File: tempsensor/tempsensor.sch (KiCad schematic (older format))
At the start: 64 parts

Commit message: Added testpads to tempsensor, added missing TWI lines to EEPROM.
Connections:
- wire segments 228 -> 241
- no-connect marks 13 -> 17
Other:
- moved on the sheet: TP?
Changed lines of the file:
@@
 L Connector:TestPoint TP?
 U 1 1 5EB7CF1E
-P 4900 5400
-F 0 "TP?" V 4854 5588 50  0000 L CNN
-F 1 "SCL" V 4945 5588 50  0000 L CNN
-F 2 "" H 5100 5400 50  0001 C CNN
-F 3 "~" H 5100 5400 50  0001 C CNN
-	1    4900 5400
+P 5450 5550
+F 0 "TP?" V 5404 5738 50  0000 L CNN
+F 1 "SCL" V 5495 5738 50  0000 L CNN
+F 2 "" H 5650 5550 50  0001 C CNN
+F 3 "~" H 5650 5550 50  0001 C CNN
+	1    5450 5550
 	0    1    1    0
 $EndComp
@@
 L Connector:TestPoint TP?
 U 1 1 5EB7D977
-P 4900 5600
-F 0 "TP?" V 4854 5788 50  0000 L CNN
-F 1 "SDA" V 4945 5788 50  0000 L CNN
-F 2 "" H 5100 5600 50  0001 C CNN
-F 3 "~" H 5100 5600 50  0001 C CNN
-	1    4900 5600
+P 5450 5750
+F 0 "TP?" V 5404 5938 50  0000 L CNN
+F 1 "SDA" V 5495 5938 50  0000 L CNN
+F 2 "" H 5650 5750 50  0001 C CNN
+F 3 "~" H 5650 5750 50  0001 C CNN
+	1    5450 5750
 	0    1    1    0
 $EndComp
@@
 L Connector:TestPoint TP?
 U 1 1 5EB7E288
-P 4900 5800
-F 0 "TP?" V 4854 5988 50  0000 L CNN
-F 1 "3V3" V 4945 5988 50  0000 L CNN
-F 2 "" H 5100 5800 50  0001 C CNN
-F 3 "~" H 5100 5800 50  0001 C CNN
-	1    4900 5800
+P 5450 5950
+F 0 "TP?" V 5404 6138 50  0000 L CNN
+F 1 "3V3" V 5495 6138 50  0000 L CNN
+F 2 "" H 5650 5950 50  0001 C CNN
+F 3 "~" H 5650 5950 50  0001 C CNN
+	1    5450 5950
 	0    1    1    0
 $EndComp
@@
 L Connector:TestPoint TP?
 U 1 1 5EB7EBA7
-P 4900 6000
-F 0 "TP?" V 4848 6188 50  0000 L CNN
-F 1 "~UVSLO" V 4946 6188 50  0000 L CNN
-F 2 "" H 5100 6000 50  0001 C CNN
-F 3 "~" H 5100 6000 50  0001 C CNN
-	1    4900 6000
+P 5450 6150
+F 0 "TP?" V 5398 6338 50  0000 L CNN
+F 1 "~UVSLO" V 5496 6338 50  0000 L CNN
+F 2 "" H 5650 6150 50  0001 C CNN
+F 3 "~" H 5650 6150 50  0001 C CNN
+	1    5450 6150
 	0    1    1    0
 $EndComp
@@
 L Connector:TestPoint TP?
 U 1 1 5EB7F4D4
-P 4900 6200
-F 0 "TP?" V 4854 6388 50  0000 L CNN
-F 1 "VDC" V 4945 6388 50  0000 L CNN
-F 2 "" H 5100 6200 50  0001 C CNN
-F 3 "~" H 5100 6200 50  0001 C CNN
-	1    4900 6200
+P 5450 6350
+F 0 "TP?" V 5404 6538 50  0000 L CNN
+F 1 "VDC" V 5495 6538 50  0000 L CNN
+F 2 "" H 5650 6350 50  0001 C CNN
+F 3 "~" H 5650 6350 50  0001 C CNN
+	1    5450 6350
 	0    1    1    0
 $EndComp
@@
 L Connector:TestPoint TP?
 U 1 1 5EB7FE0F
-P 4900 6400
-F 0 "TP?" V 4854 6588 50  0000 L CNN
-F 1 "VBUS" V 4945 6588 50  0000 L CNN
-F 2 "" H 5100 6400 50  0001 C CNN
-F 3 "~" H 5100 6400 50  0001 C CNN
-	1    4900 6400
+P 5450 6550
+F 0 "TP?" V 5404 6738 50  0000 L CNN
+F 1 "VBUS" V 5495 6738 50  0000 L CNN
+F 2 "" H 5650 6550 50  0001 C CNN
+F 3 "~" H 5650 6550 50  0001 C CNN
+	1    5450 6550
 	0    1    1    0
 $EndComp
@@
 L Connector:TestPoint TP?
 U 1 1 5EB80758
-P 4900 6600
-F 0 "TP?" V 4854 6788 50  0000 L CNN
-F 1 "GND" V 4945 6788 50  0000 L CNN
-F 2 "" H 5100 6600 50  0001 C CNN
-F 3 "~" H 5100 6600 50  0001 C CNN
-	1    4900 6600
+P 5450 6750
+F 0 "TP?" V 5404 6938 50  0000 L CNN
+F 1 "GND" V 5495 6938 50  0000 L CNN
+F 2 "" H 5650 6750 50  0001 C CNN
+F 3 "~" H 5650 6750 50  0001 C CNN
+	1    5450 6750
 	0    1    1    0
 $EndComp
@@
 L Connector:TestPoint TP?
 U 1 1 5EBA1FF2
-P 4900 6800
-F 0 "TP?" V 4854 6988 50  0000 L CNN
-F 1 "RXD" V 4945 6988 50  0000 L CNN
-F 2 "" H 5100 6800 50  0001 C CNN
-F 3 "~" H 5100 6800 50  0001 C CNN
-	1    4900 6800
+P 5450 6950
+F 0 "TP?" V 5404 7138 50  0000 L CNN
+F 1 "RXD" V 5495 7138 50  0000 L CNN
+F 2 "" H 5650 6950 50  0001 C CNN
+F 3 "~" H 5650 6950 50  0001 C CNN
+	1    5450 6950
 	0    1    1    0
 $EndComp
@@
 L Connector:TestPoint TP?
 U 1 1 5EBA20D8
-P 4900 7000
-F 0 "TP?" V 4854 7188 50  0000 L CNN
-F 1 "TXD" V 4945 7188 50  0000 L CNN
-F 2 "" H 5100 7000 50  0001 C CNN
-F 3 "~" H 5100 7000 50  0001 C CNN
-	1    4900 7000
+P 5450 7150
+F 0 "TP?" V 5404 7338 50  0000 L CNN
+F 1 "TXD" V 5495 7338 50  0000 L CNN
+F 2 "" H 5650 7150 50  0001 C CNN
+F 3 "~" H 5650 7150 50  0001 C CNN
+	1    5450 7150
 	0    1    1    0
 $EndComp
@@
 L Connector:TestPoint TP?
 U 1 1 5EBA21BE
-P 4900 7200
-F 0 "TP?" V 4854 7388 50  0000 L CNN
-F 1 "DTR" V 4945 7388 50  0000 L CNN
-F 2 "" H 5100 7200 50  0001 C CNN
-F 3 "~" H 5100 7200 50  0001 C CNN
-	1    4900 7200
+P 5450 7350
+F 0 "TP?" V 5404 7538 50  0000 L CNN
+F 1 "DTR" V 5495 7538 50  0000 L CNN
+F 2 "" H 5650 7350 50  0001 C CNN
+F 3 "~" H 5650 7350 50  0001 C CNN
+	1    5450 7350
 	0    1    1    0
 $EndComp
@@
 L Connector:TestPoint TP?
 U 1 1 5EBA22A4
-P 4900 7400
-F 0 "TP?" V 4854 7588 50  0000 L CNN
-F 1 "RTS" V 4945 7588 50  0000 L CNN
-F 2 "" H 5100 7400 50  0001 C CNN
-F 3 "~" H 5100 7400 50  0001 C CNN
-	1    4900 7400
+P 5450 7550
+F 0 "TP?" V 5404 7738 50  0000 L CNN
+F 1 "RTS" V 5495 7738 50  0000 L CNN
+F 2 "" H 5650 7550 50  0001 C CNN
+F 3 "~" H 5650 7550 50  0001 C CNN
+	1    5450 7550
 	0    1    1    0
 $EndComp
@@
 Wire Notes Line
 	9950 1050 9950 3100
+NoConn ~ 6950 2250
+NoConn ~ 5000 1600
+NoConn ~ 5000 1700
+NoConn ~ 5000 1800
+Text Label 3200 3500 2    50   ~ 0
+SDA
+Wire Wire Line
+	3200 3500 3100 3500
+Text Label 3200 3600 2    50   ~ 0
+SCL
+Wire Wire Line
+	3200 3600 3100 3600
+Text Label 5150 6150 0    50   ~ 0
+~UVSLO
+Wire Wire Line
+	5150 6150 5450 6150
+Text Label 5150 5550 0    50   ~ 0
+SCL
+Wire Wire Line
+	5150 5550 5450 5550
+Text Label 5150 5750 0    50   ~ 0
+SDA
+$Comp
+L power:+3.3V #PWR?
+U 1 1 5ED29DE4
+P 5400 5950
+F 0 "#PWR?" H 5400 5800 50  0001 C CNN
+F 1 "+3.3V" V 5415 6078 50  0000 L CNN
+F 2 "" H 5400 5950 50  0001 C CNN
+F 3 "" H 5400 5950 50  0001 C CNN
+	1    5400 5950
+	0    -1   -1   0
+$EndComp
+$Comp
+L power:+VDC #PWR?
+U 1 1 5ED2AB33
+P 5400 6350
+F 0 "#PWR?" H 5400 6250 50  0001 C CNN
+F 1 "+VDC" V 5400 6579 50  0000 L CNN
+F 2 "" H 5400 6350 50  0001 C CNN
+F 3 "" H 5400 6350 50  0001 C CNN
+	1    5400 6350
+	0    -1   -1   0
+$EndComp
+$Comp
+L power:VBUS #PWR?
+U 1 1 5ED2B80A
+P 5400 6550
+F 0 "#PWR?" H 5400 6400 50  0001 C CNN
+F 1 "VBUS" V 5415 6677 50  0000 L CNN
+F 2 "" H 5400 6550 50  0001 C CNN
+F 3 "" H 5400 6550 50  0001 C CNN
+	1    5400 6550
+	0    -1   -1   0
+$EndComp
+$Comp
+L power:GND #PWR?
+U 1 1 5ED2C458
+P 5400 6750
+F 0 "#PWR?" H 5400 6500 50  0001 C CNN
+F 1 "GND" V 5405 6622 50  0000 R CNN
+F 2 "" H 5400 6750 50  0001 C CNN
+F 3 "" H 5400 6750 50  0001 C CNN
+	1    5400 6750
+	0    1    1    0
+$EndComp
+Text Label 5150 6950 0    50   ~ 0
+RXD
+Text Label 5150 7150 0    50   ~ 0
+TXD
+Text Label 5150 7350 0    50   ~ 0
+DTR
+Text Label 5150 7550 0    50   ~ 0
+RTS
+Wire Wire Line
+	5450 7350 5150 7350
+Wire Wire Line
+	5450 7550 5150 7550
+Wire Wire Line
+	5150 7150 5450 7150
+Wire Wire Line
+	5150 6950 5450 6950
+Wire Wire Line
+	5400 6750 5450 6750
+Wire Wire Line
+	5400 6550 5450 6550
+Wire Wire Line
+	5400 6350 5450 6350
+Wire Wire Line
+	5400 5950 5450 5950
+Wire Wire Line
+	5150 5750 5450 5750
 $EndSCHEMATC

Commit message: Removed OP-AMP from tempsensor, not really needed.
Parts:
- removed C?: 10n, symbol Device:C
- removed U? (x3): LM358, symbol Amplifier_Operational:LM358
- C?: value 1n -> 10n
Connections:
- wire segments 241 -> 223
- no-connect marks 17 -> 16
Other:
- moved on the sheet: D?, R?
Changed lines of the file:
@@
 L Device:R R?
 U 1 1 5E78BBCC
-P 2100 1100
-F 0 "R?" H 2170 1146 50  0000 L CNN
-F 1 "430K" H 2170 1055 50  0000 L CNN
-F 2 "" V 2030 1100 50  0001 C CNN
-F 3 "~" H 2100 1100 50  0001 C CNN
-	1    2100 1100
+P 2100 1200
+F 0 "R?" H 2170 1246 50  0000 L CNN
+F 1 "430K" H 2170 1155 50  0000 L CNN
+F 2 "" V 2030 1200 50  0001 C CNN
+F 3 "~" H 2100 1200 50  0001 C CNN
+	1    2100 1200
 	1    0    0    -1
 $EndComp
@@
 L Device:R R?
 U 1 1 5E78C20B
-P 2100 1500
-F 0 "R?" H 2170 1546 50  0000 L CNN
-F 1 "100K" H 2170 1455 50  0000 L CNN
-F 2 "" V 2030 1500 50  0001 C CNN
-F 3 "~" H 2100 1500 50  0001 C CNN
-	1    2100 1500
+P 2100 1600
+F 0 "R?" H 2170 1646 50  0000 L CNN
+F 1 "100K" H 2170 1555 50  0000 L CNN
+F 2 "" V 2030 1600 50  0001 C CNN
+F 3 "~" H 2100 1600 50  0001 C CNN
+	1    2100 1600
 	1    0    0    -1
 $EndComp
@@
 $EndComp
 Wire Wire Line
-	2100 2350 2100 1650
+	2100 2350 2100 1750
 $Comp
 L power:+BATT #PWR?
@@
 $EndComp
 Wire Wire Line
-	2100 750  2100 950
-Wire Wire Line
-	2100 1250 2100 1300
-$Comp
-L Amplifier_Operational:LM358 U?
-U 1 1 5E799684
-P 3350 1400
-F 0 "U?" H 3350 1767 50  0000 C CNN
-F 1 "LM358" H 3350 1676 50  0000 C CNN
-F 2 "" H 3350 1400 50  0001 C CNN
-F 3 "http://www.ti.com/lit/ds/symlink/lm2904-n.pdf" H 3350 1400 50  0001 C CNN
-	1    3350 1400
-	1    0    0    -1
-$EndComp
-Wire Wire Line
-	3700 1400 3700 1650
-Wire Wire Line
-	3700 1650 3350 1650
-Wire Wire Line
-	3000 1650 3000 1500
-Wire Wire Line
-	3000 1500 3050 1500
-Wire Wire Line
-	3650 1400 3700 1400
-Connection ~ 3700 1400
-Wire Wire Line
-	3700 1400 3800 1400
-Connection ~ 2100 1300
-Wire Wire Line
-	2100 1300 2100 1350
+	2100 750  2100 1050
+Wire Wire Line
+	2100 1350 2100 1400
+Connection ~ 2100 1400
+Wire Wire Line
+	2100 1400 2100 1450
 $Comp
 L Device:D_Zener D?
 U 1 1 5E7AED8C
-P 2550 1500
-F 0 "D?" V 2504 1580 50  0000 L CNN
-F 1 "ZMM3V3" V 2595 1580 50  0000 L CNN
-F 2 "" H 2550 1500 50  0001 C CNN
-F 3 "~" H 2550 1500 50  0001 C CNN
-	1    2550 1500
-	0    1    1    0
-$EndComp
-Wire Wire Line
-	2100 1300 2550 1300
-Wire Wire Line
-	2550 1350 2550 1300
-Connection ~ 2550 1300
-Wire Wire Line
-	2550 1300 3050 1300
+P 2550 1850
+F 0 "D?" V 2504 1930 50  0000 L CNN
+F 1 "ZMM3V3" V 2595 1930 50  0000 L CNN
+F 2 "" H 2550 1850 50  0001 C CNN
+F 3 "~" H 2550 1850 50  0001 C CNN
+	1    2550 1850
+	0    1    1    0
+$EndComp
+Wire Wire Line
+	2100 1400 2550 1400
+Wire Wire Line
+	2550 1700 2550 1400
 $Comp
 L power:GND #PWR?
@@
 $EndComp
 Wire Wire Line
-	2550 1650 2550 2350
+	2550 2000 2550 2350
 $Comp
 L Device:C C?
@@
 P 3350 1850
 F 0 "C?" H 3465 1896 50  0000 L CNN
-F 1 "1n" H 3465 1805 50  0000 L CNN
+F 1 "10n" H 3465 1805 50  0000 L CNN
 F 2 "" H 3388 1700 50  0001 C CNN
 F 3 "~" H 3350 1850 50  0001 C CNN
@@
 	1    0    0    -1
 $EndComp
-Wire Wire Line
-	3350 1700 3350 1650
-Connection ~ 3350 1650
-Wire Wire Line
-	3350 1650 3000 1650
 $Comp
 L power:GND #PWR?
@@
 Wire Notes Line
 	1350 5850 2800 5850
-$Comp
-L Amplifier_Operational:LM358 U?
-U 2 1 5EC38D07
-P 10500 1500
-F 0 "U?" H 10500 1867 50  0000 C CNN
-F 1 "LM358" H 10500 1776 50  0000 C CNN
-F 2 "" H 10500 1500 50  0001 C CNN
-F 3 "http://www.ti.com/lit/ds/symlink/lm2904-n.pdf" H 10500 1500 50  0001 C CNN
-	2    10500 1500
-	1    0    0    -1
-$EndComp
-$Comp
-L Amplifier_Operational:LM358 U?
-U 3 1 5EC3A76F
-P 10650 2450
-F 0 "U?" H 10608 2496 50  0000 L CNN
-F 1 "LM358" H 10608 2405 50  0000 L CNN
-F 2 "" H 10650 2450 50  0001 C CNN
-F 3 "http://www.ti.com/lit/ds/symlink/lm2904-n.pdf" H 10650 2450 50  0001 C CNN
-	3    10650 2450
-	1    0    0    -1
-$EndComp
-$Comp
-L Device:C C?
-U 1 1 5EC3D0DD
-P 10150 2450
-F 0 "C?" H 10265 2496 50  0000 L CNN
-F 1 "10n" H 10265 2405 50  0000 L CNN
-F 2 "" H 10188 2300 50  0001 C CNN
-F 3 "~" H 10150 2450 50  0001 C CNN
-	1    10150 2450
-	1    0    0    -1
-$EndComp
-$Comp
-L power:+3.3V #PWR?
-U 1 1 5EC3E112
-P 10550 2050
-F 0 "#PWR?" H 10550 1900 50  0001 C CNN
-F 1 "+3.3V" H 10565 2223 50  0000 C CNN
-F 2 "" H 10550 2050 50  0001 C CNN
-F 3 "" H 10550 2050 50  0001 C CNN
-	1    10550 2050
-	1    0    0    -1
-$EndComp
-Wire Wire Line
-	10550 2050 10550 2100
-Wire Wire Line
-	10550 2100 10150 2100
-Wire Wire Line
-	10150 2100 10150 2300
-Connection ~ 10550 2100
-Wire Wire Line
-	10550 2100 10550 2150
-Wire Wire Line
-	10150 2600 10150 2800
-Wire Wire Line
-	10150 2800 10550 2800
-Wire Wire Line
-	10550 2800 10550 2750
-$Comp
-L power:GND #PWR?
-U 1 1 5EC68906
-P 10550 2850
-F 0 "#PWR?" H 10550 2600 50  0001 C CNN
-F 1 "GND" H 10555 2677 50  0000 C CNN
-F 2 "" H 10550 2850 50  0001 C CNN
-F 3 "" H 10550 2850 50  0001 C CNN
-	1    10550 2850
-	1    0    0    -1
-$EndComp
-Wire Wire Line
-	10550 2850 10550 2800
-Connection ~ 10550 2800
-NoConn ~ 10800 1500
-$Comp
-L power:GND #PWR?
-U 1 1 5EC85152
-P 10150 1650
-F 0 "#PWR?" H 10150 1400 50  0001 C CNN
-F 1 "GND" H 10155 1477 50  0000 C CNN
-F 2 "" H 10150 1650 50  0001 C CNN
-F 3 "" H 10150 1650 50  0001 C CNN
-	1    10150 1650
-	1    0    0    -1
-$EndComp
-Wire Wire Line
-	10150 1650 10150 1600
-Wire Wire Line
-	10150 1400 10200 1400
-Wire Wire Line
-	10200 1600 10150 1600
-Connection ~ 10150 1600
-Wire Wire Line
-	10150 1600 10150 1400
-Wire Notes Line
-	9950 1050 10900 1050
-Wire Notes Line
-	10900 1050 10900 3100
-Wire Notes Line
-	10900 3100 9950 3100
-Wire Notes Line
-	9950 1050 9950 3100
 NoConn ~ 6950 2250
 NoConn ~ 5000 1600
@@
 Wire Wire Line
 	5150 5750 5450 5750
+Wire Wire Line
+	2550 1400 3350 1400
+Connection ~ 2550 1400
+Wire Wire Line
+	3350 1700 3350 1400
+Connection ~ 3350 1400
+Wire Wire Line
+	3350 1400 3800 1400
 $EndSCHEMATC

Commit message: Changed Tempsensor power-on circuit to use the enable pin of the step-down converter. Added some footprints.
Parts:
- removed D?: ZMM3V3, symbol Device:D_Zener
- removed Q?: BC807, Package_TO_SOT_SMD:SOT-23, symbol Transistor_BJT:BC807
- removed Q?: 2N7002K, Package_TO_SOT_SMD:SOT-23, symbol Transistor_FET:2N7002K
- removed R?: R, symbol Device:R
- removed R?: 1M, symbol Device:R
- added D?: D, symbol Device:D
- added D?: ZMM3V3, symbol Device:D_Zener
- added R?: 100K, Resistor_SMD:R_0603_1608Metric, symbol Device:R
- added R? (x2): 10K, Resistor_SMD:R_0603_1608Metric, symbol Device:R
- added SW?: PW_OFF, symbol Switch:SW_Push
- added TP?: BAT+, symbol Connector:TestPoint
- D? (x2): footprint (none) -> LED_SMD:LED_1210_3225Metric
- J?: footprint (none) -> myfootprints:USB-Mini-B_Wuerth_651005136521_Horizontal
- L?: footprint (none) -> Inductor_SMD:L_1210_3225Metric
- R? (x17): footprint (none) -> Resistor_SMD:R_0603_1608Metric
- SW?: value SW_Push -> PW_ON
- U?: footprint (none) -> Package_SO:SOIC-16W_7.5x10.3mm_P1.27mm
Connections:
- wire segments 223 -> 224
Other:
- note added: "Battery Disconnect\nWhen charger is connected,\nVBUS voltage is higher than +BATT\nLoad still supplied from\nUSB, but not from battery"
- note added: "ESP-12F"
- note added: "Testpointsfor verification and programming"
- note added: "USB Connector\nfor charging only"
- note removed: "Battery Disconnect\nWhen charger is connected,\ndisconnect load from Battery.\nLoad still supplied from\nUSB"
- note removed: "USB Connector"
- moved on the sheet: C?, D?, J?, L?, Q?, R?, SW?, TP?, U?

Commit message: Added remaining footprints to thermosthat, redesigned self-turn-off circuit of tempsensor.
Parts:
- added R7: 10K, Resistor_SMD:R_0603_1608Metric, symbol Device:R
- U6: renamed from U?; symbol Regulator_Switching:MAX17620 -> tempsensor-rescue:MAX17620-Regulator_Switching
- gave numbers to parts that had none: 61
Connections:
- wire segments 224 -> 225

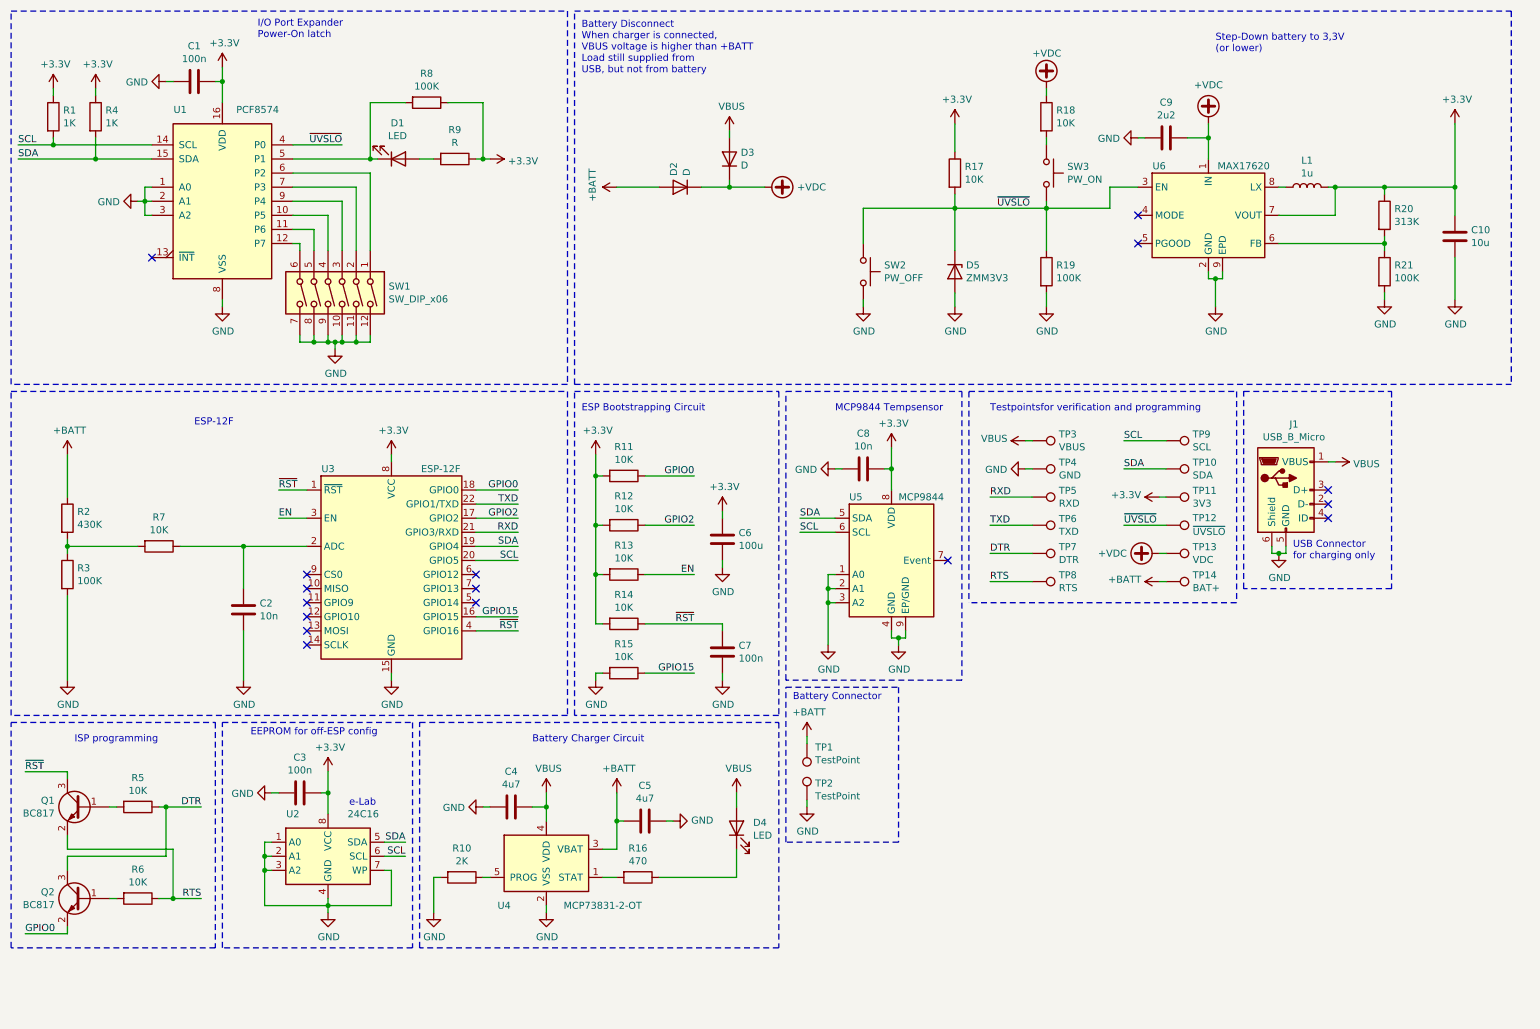
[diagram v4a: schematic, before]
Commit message: Added interrupt circuit to tempsensor MCP9844 to allow it to wake up ESP on temperature changes (so that I can program thresholds instead of waking up more often).
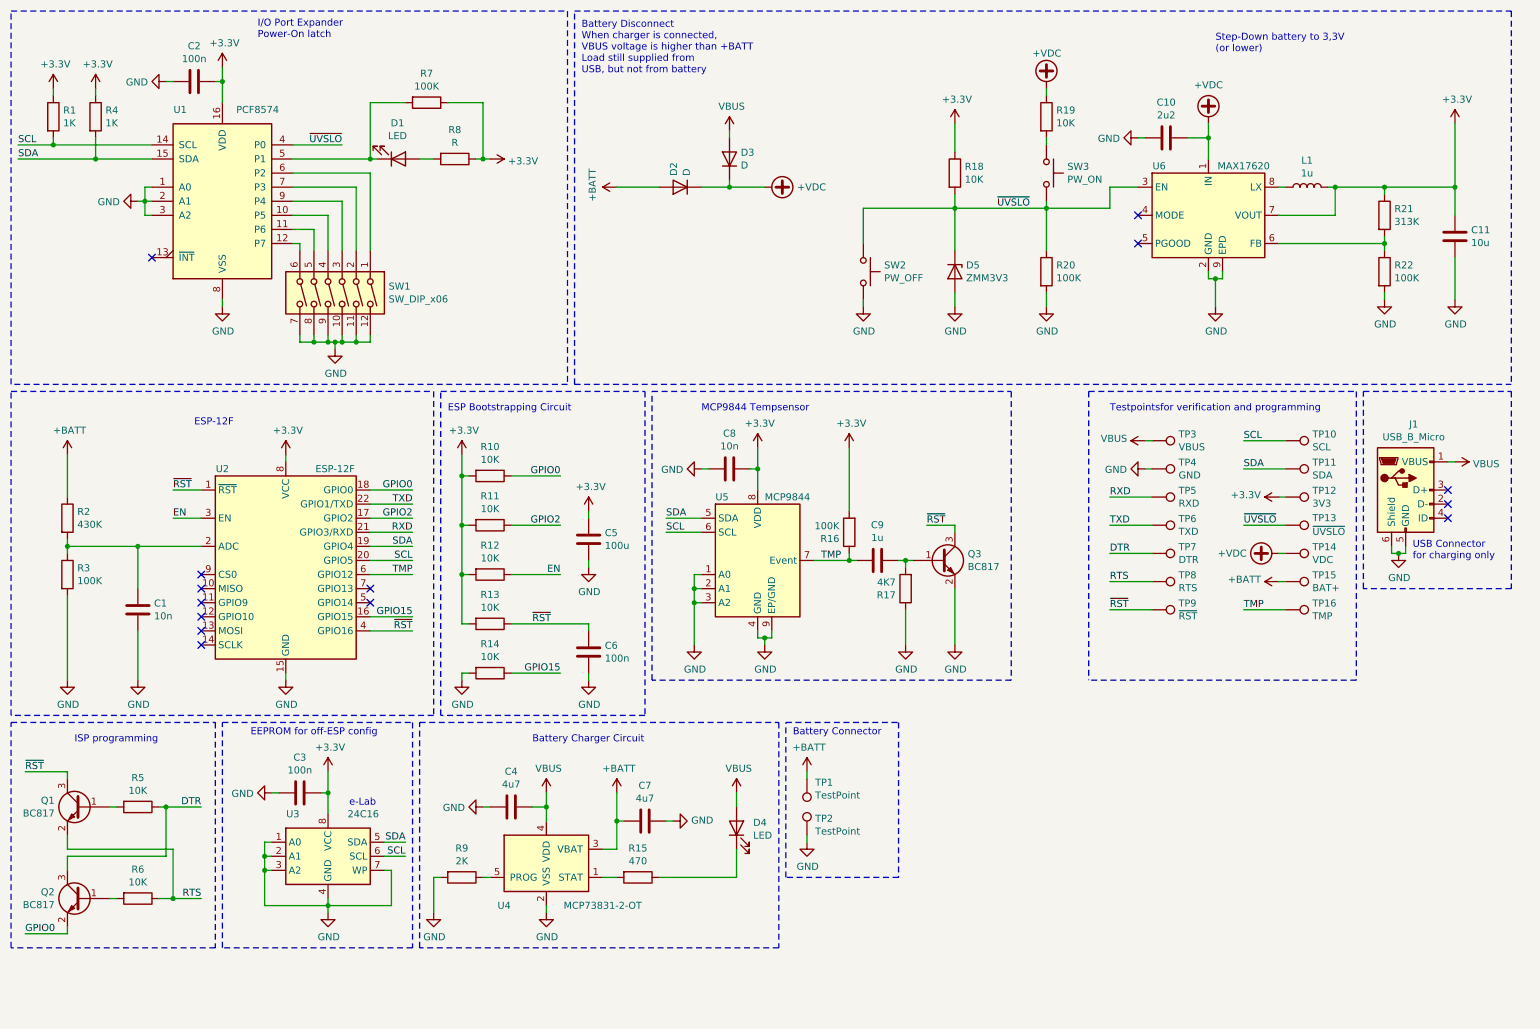
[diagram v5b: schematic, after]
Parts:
- removed R7: 10K, Resistor_SMD:R_0603_1608Metric, symbol Device:R
- added C9: 1u, symbol Device:C
- added Q3: BC817, Package_TO_SOT_SMD:SOT-23, symbol Transistor_BJT:BC817
- added R16: 100K, Resistor_SMD:R_0603_1608Metric, symbol Device:R
- added R17: 4K7, Resistor_SMD:R_0603_1608Metric, symbol Device:R
- added TP16: TMP, symbol Connector:TestPoint
- added TP9: ~RST, symbol Connector:TestPoint
- renumbered C2 to C1, C9 to C10, C10 to C11, C1 to C2, C6 to C5, C7 to C6, C5 to C7, R11 to R10, R12 to R11, R13 to R12, R14 to R13, R15 to R14, R16 to R15, R17 to R18, R18 to R19, R19 to R20, R20 to R21, R21 to R22, R8 to R7, R9 to R8, R10 to R9, TP9 to TP10, TP10 to TP11, TP11 to TP12, TP12 to TP13, TP13 to TP14, TP14 to TP15, U3 to U2, U2 to U3
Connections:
- net +3V3: now also R16.2
- net GND: now also Q3.2 (E), R17.1
- net ~RST: now also Q3.3 (C), TP9.1
- net at C1.1, U2.2 (ADC): now also R2.2, R3.1
- net TMP: now reaches U2.6 (GPIO12)
- net TMP: now also U5.7 (Event), C9.2, R16.1, TP16.1
- new net: C9.1, Q3.1 (B), R17.2
- no-connect marks 16 -> 14
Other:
- moved on the sheet: C1, C5, C6, C8, J1, R10, R11, R12, R13, R14, TP1, TP10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
